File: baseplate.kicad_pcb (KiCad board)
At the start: 2 copper layers, 32 x 32 mm, 12 parts, among them M1 THRU_HOLE_PAD, M2 THRU_HOLE_PAD, M3 THRU_HOLE_PAD, M4 THRU_HOLE_PAD, M5 THRU_HOLE_PAD, M6 THRU_HOLE_PAD, M7 THRU_HOLE_PAD, U1 STM32L011F4Ux, U3 DF52-4S-0.8H(21)

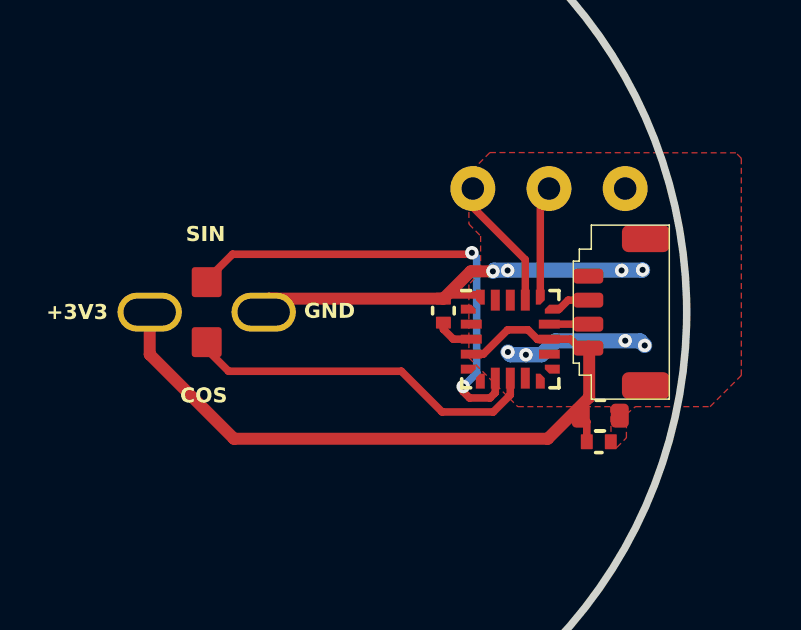
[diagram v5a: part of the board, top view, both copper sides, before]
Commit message: step files from freecad, put the connector on the baseplate on the bottom of the baseplate
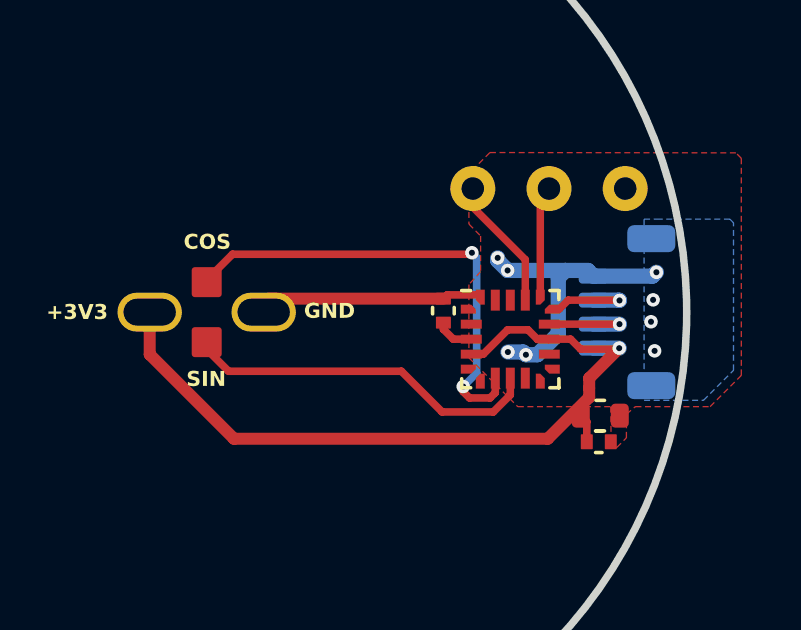
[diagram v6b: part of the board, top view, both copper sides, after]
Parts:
- removed U3: DF52-4S-0.8H(21), foc-pcb-library:DF52-4S-0.8H(21)
- added U2: DF52-4S-0.8H(21), foc-pcb-library:DF52-4S-0.8H(21), B.Cu at (156.3, 102.1)
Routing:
- net +3V3: track 24.9 -> 27.2 mm, vias 0 -> 1
- net GND: track 19.5 -> 17.5 mm
- net /RX: track 1.25 -> 3.16 mm, vias 0 -> 1
- net /TX: track 1.30 -> 3.20 mm, vias 0 -> 1
- added copper zone on B.Cu, net GND
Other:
- board text added: "3V3"
- board text added: "RX"
- board text added: "TX"

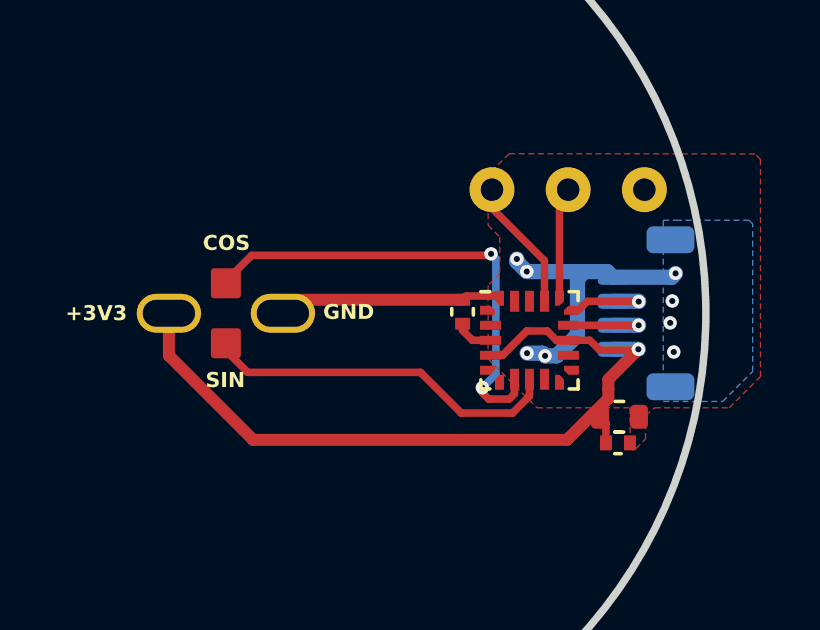
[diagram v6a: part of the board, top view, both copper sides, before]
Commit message: reverted baseplate back to all on top, designed to flip over, and solder from the component side. dogbone bottom changed so one end has three prongs
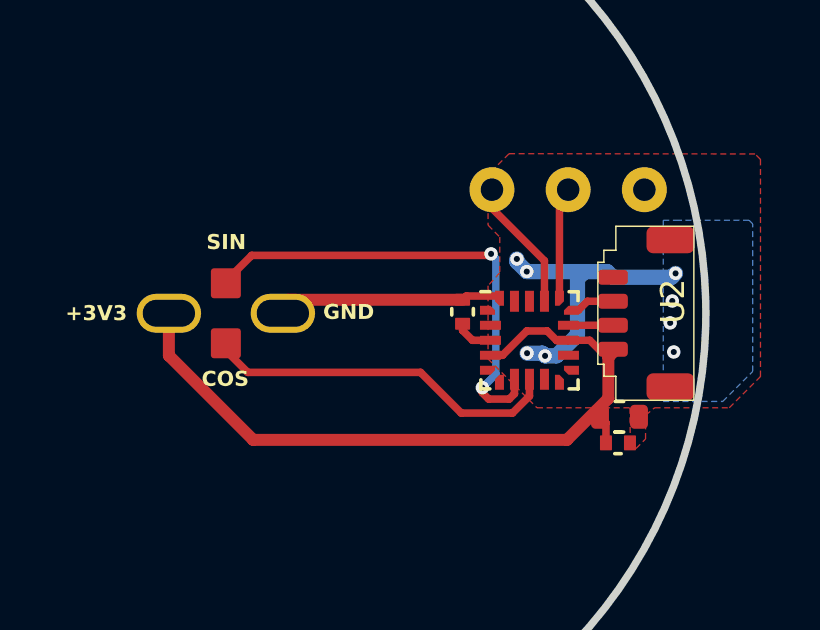
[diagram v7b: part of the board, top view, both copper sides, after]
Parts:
- added M1: THRU_HOLE_PAD, adapter-encoder:dogbone_slot, F.Cu at (143.4, 102.1)
- U2: moved to F.Cu
- turned U2 to 90 degrees
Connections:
- M2 pad 1: /COS -> /SIN
- M3 pad 1: /SIN -> /COS
- U1 pad 7: /COS -> /SIN
- U1 pad 8: /SIN -> /COS
- U2 pad 1: GND -> +3V3
- U2 pad 2: /RX -> /TX
- U2 pad 3: /TX -> /RX
- U2 pad 4: +3V3 -> GND
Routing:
- net /SIN: track 12.0 -> 15.9 mm, vias 0 -> 2
- net /COS: track 15.9 -> 12.0 mm, vias 2 -> 0
- net +3V3: track 27.2 -> 25.2 mm, vias 1 -> 0
- net /TX: track 3.20 -> 1.52 mm, vias 1 -> 0
- net /RX: track 3.16 -> 1.50 mm, vias 1 -> 0

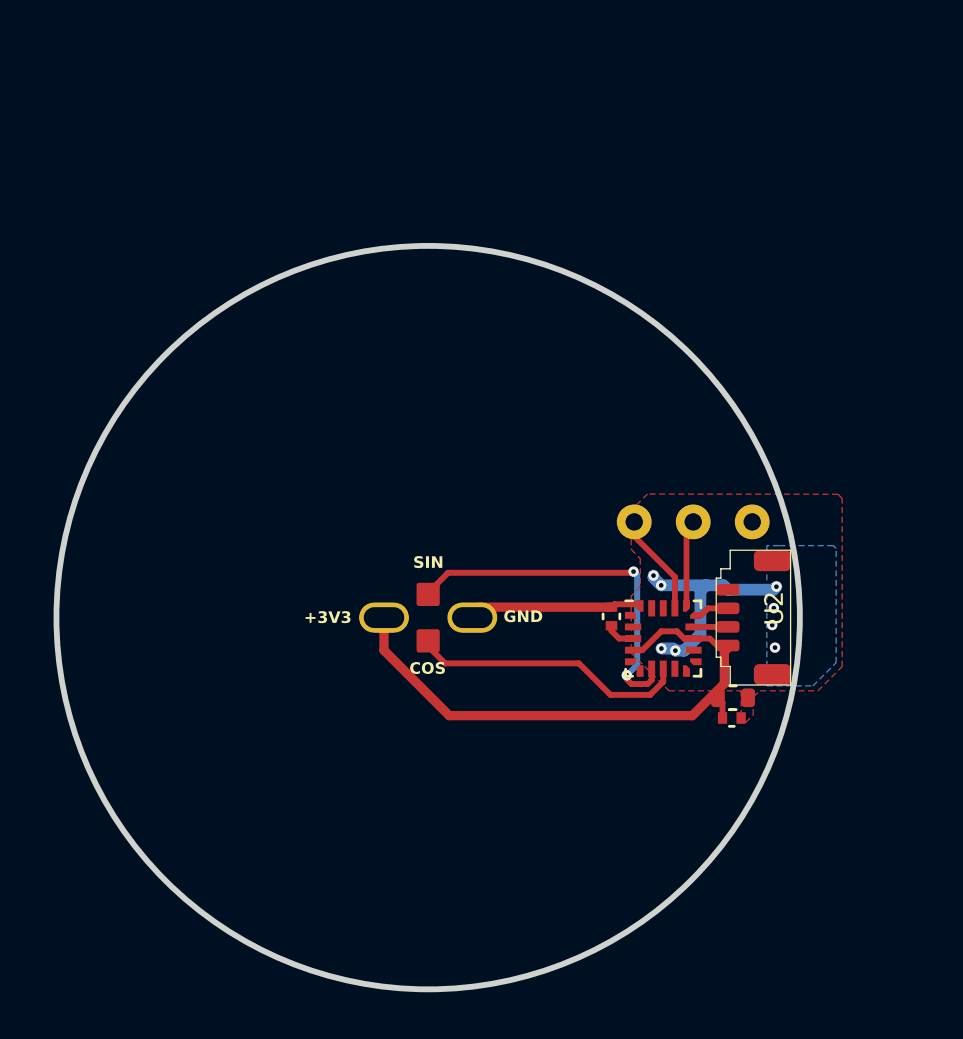
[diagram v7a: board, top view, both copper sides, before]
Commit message: updated baseplate dsign
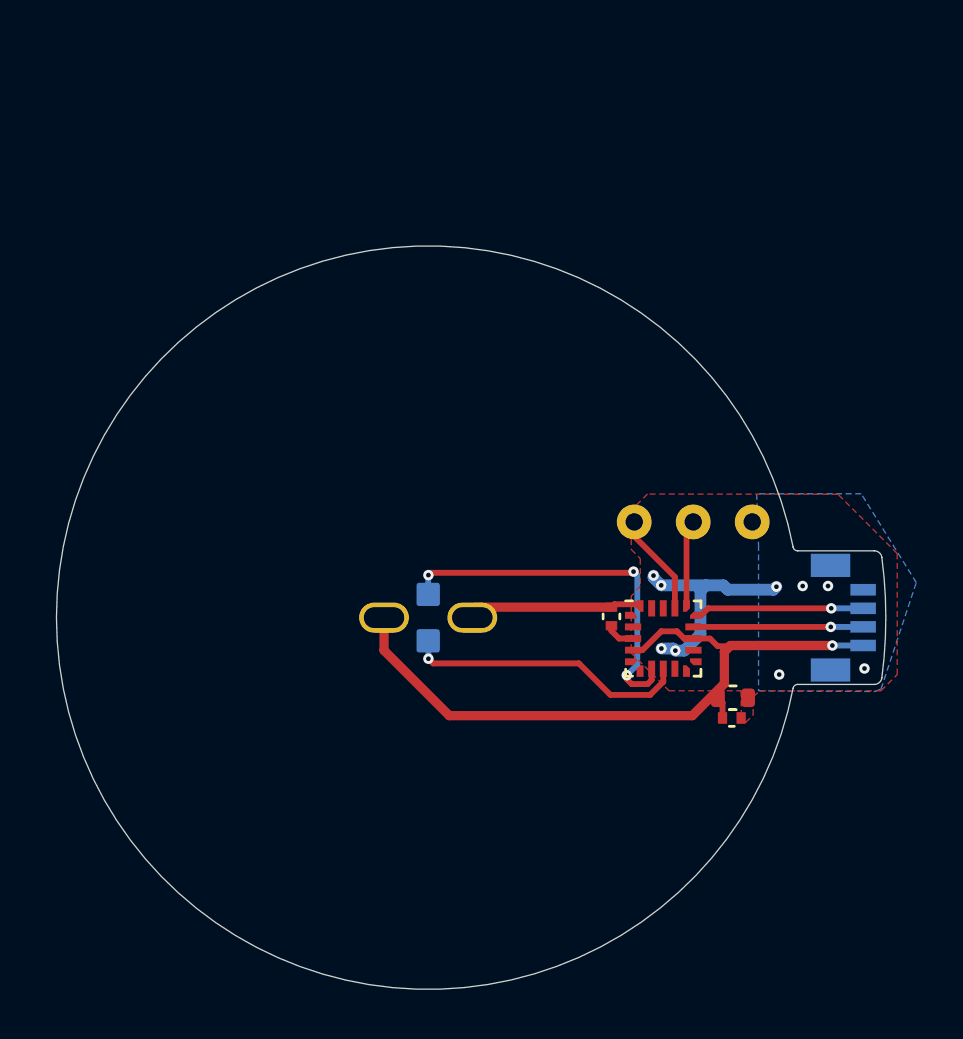
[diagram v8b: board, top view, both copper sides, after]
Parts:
- removed U2: DF52-4S-0.8H(21), foc-pcb-library:DF52-4S-0.8H(21)
- added J1: 10144042-04011LF, adapter-encoder:AMPHENOL_10144042-04011LF, B.Cu at (162.1, 102.1)
- M2, M3: moved to B.Cu
- turned M2 to 180 degrees
- turned M3 to 180 degrees
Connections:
- M2 pad 1: /SIN -> /COS
- M3 pad 1: /COS -> /SIN
- U1 pad 7: /SIN -> /COS
- U1 pad 8: /COS -> /SIN
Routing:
- net +3V3: track 25.2 -> 31.3 mm, vias 0 -> 1
- net /RX: track 1.50 -> 7.35 mm, vias 0 -> 1
- net /TX: track 1.52 -> 7.30 mm, vias 0 -> 1
- net /COS: track 12.0 -> 16.3 mm, vias 0 -> 3
- net /SIN: track 15.9 -> 12.3 mm, vias 2 -> 1
- net GND: vias 8 -> 9
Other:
- board size 32 x 32 mm -> 35.7 x 32 mm
- board text added: "SWCLK"
- board text added: "SWDIO"
